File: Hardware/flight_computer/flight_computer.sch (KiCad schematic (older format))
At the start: 38 parts, among them J1 Micro_USB, J2 MicroSD_molex, J3 rpi_zero_w, Q1 PMOS_20V_.76A, Q2 PMOS_20V_.76A, U1 FRAM_128K, U2 STM32F427VITx, U3 MCP131T-300E_TT, Y1 Crystal_24MHZ

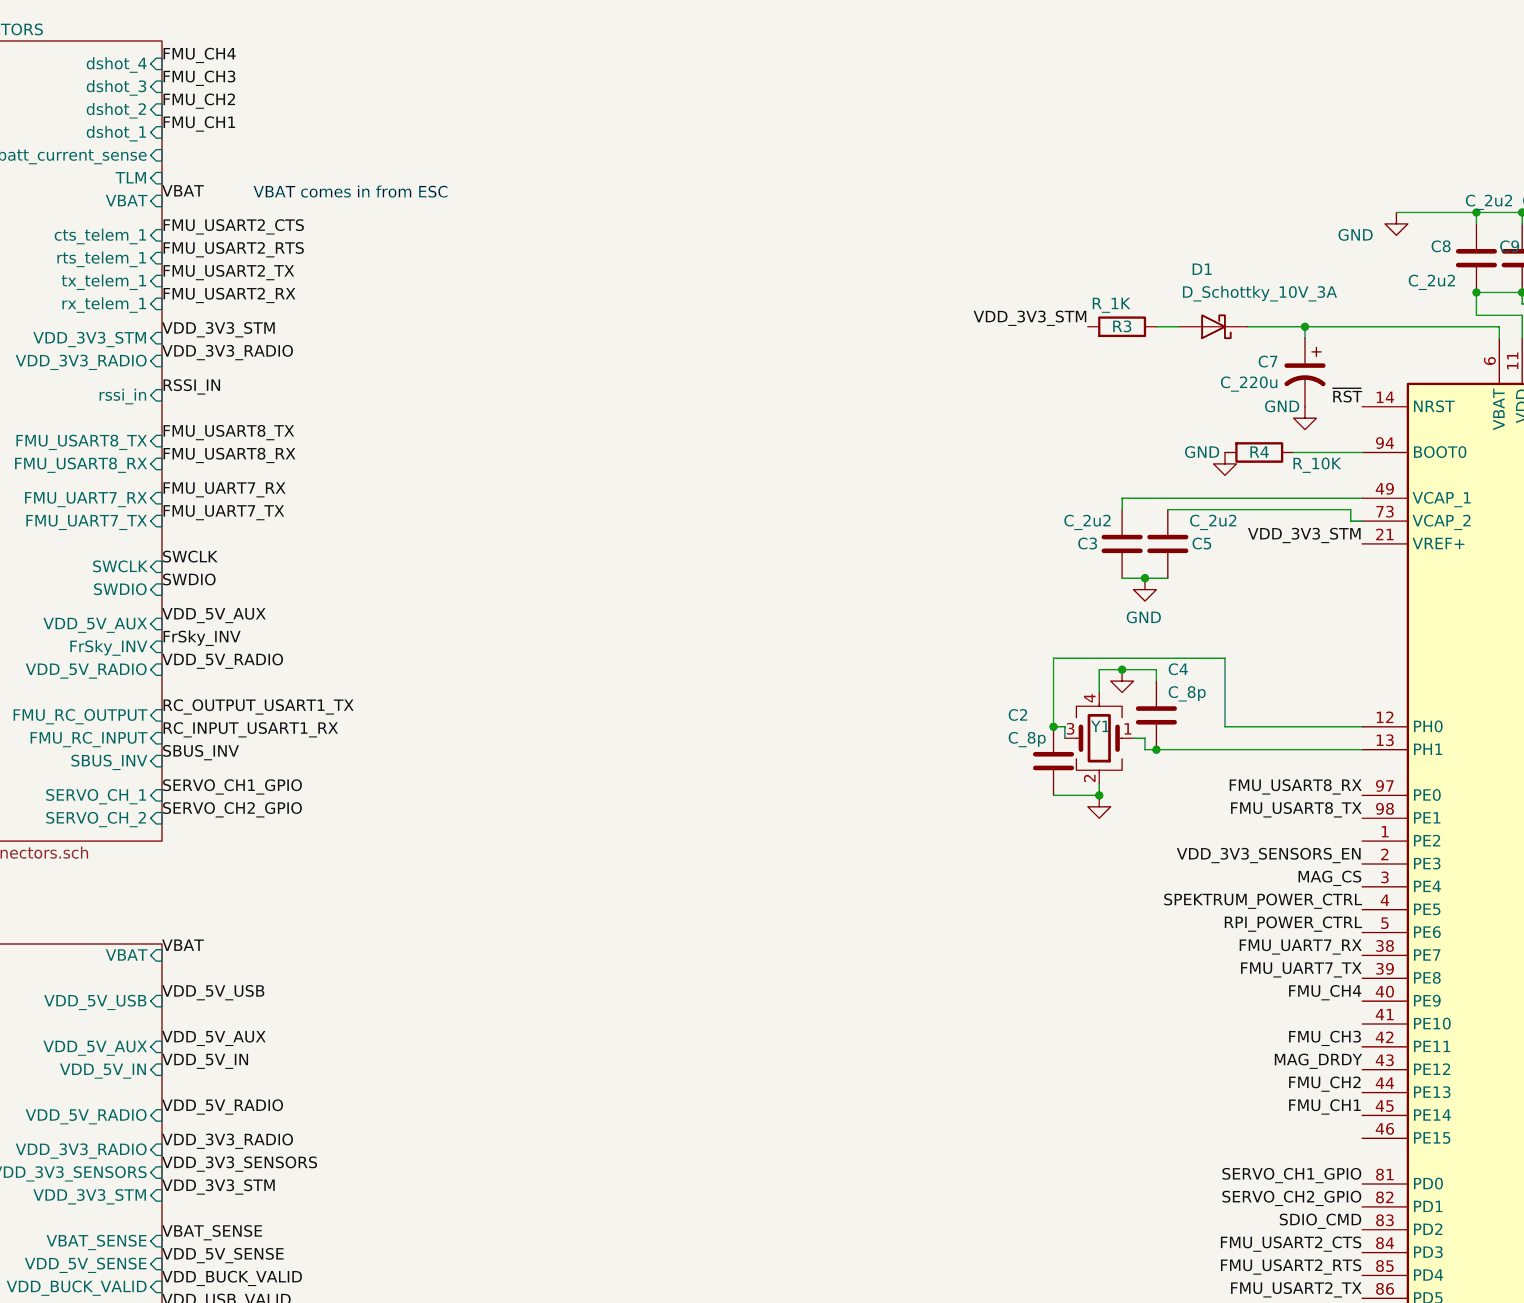
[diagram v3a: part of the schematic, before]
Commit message: Adds remainder esc gpio connections
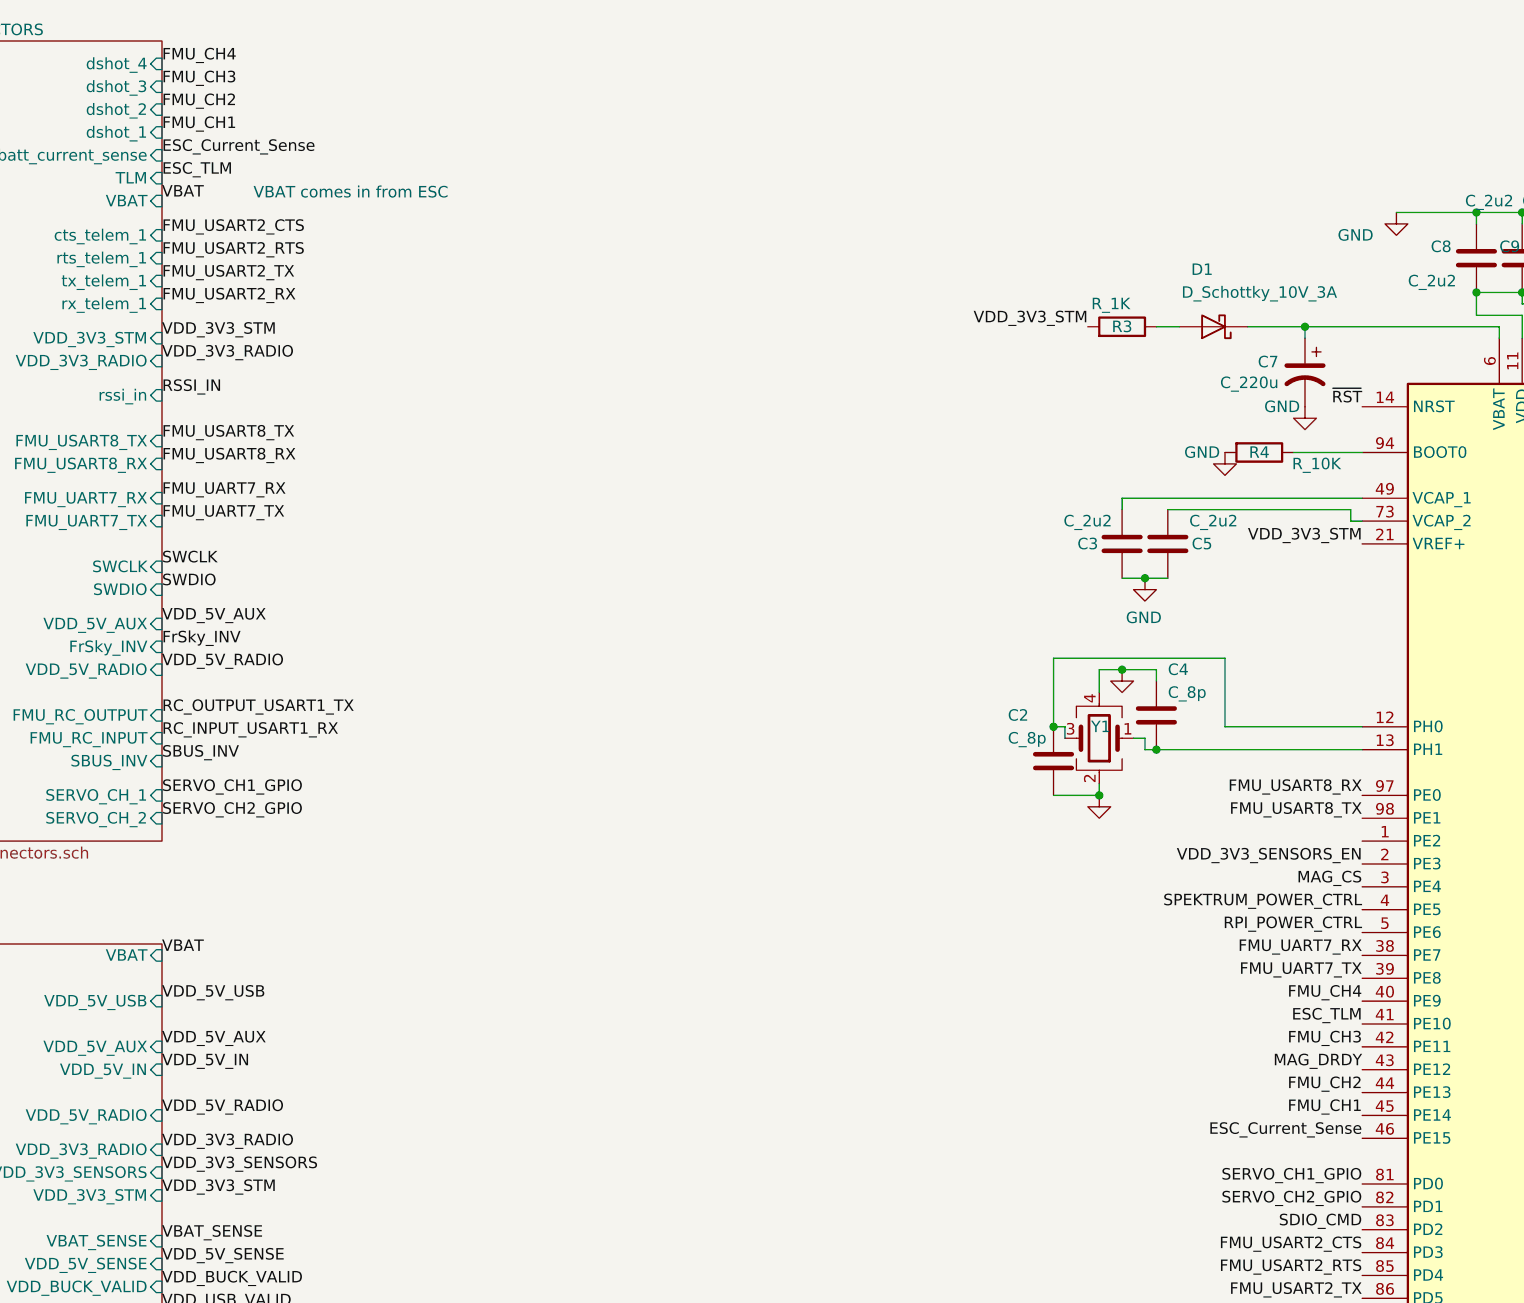
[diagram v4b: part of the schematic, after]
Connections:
- net ESC_TLM: now reaches U2.41 (PE10)
- net ESC_Current_Sense: now reaches U2.46 (PE15)
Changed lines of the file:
@@
 F16 "SWCLK" I R 1700 3000 50
 F17 "SWDIO" I R 1700 3100 50
-F19 "FMU_USART8_TX" I R 1700 2450 50
-F20 "FMU_USART8_RX" I R 1700 2550 50
-F21 "FrSky_INV" I R 1700 3350 50
-F22 "FMU_RC_OUTPUT" I R 1700 3650 50
-F23 "FMU_RC_INPUT" I R 1700 3750 50
-F24 "SBUS_INV" I R 1700 3850 50
-F25 "VDD_5V_RADIO" I R 1700 3450 50
-F26 "VDD_5V_AUX" I R 1700 3250 50
-F27 "SERVO_CH_1" I R 1700 4000 50
-F28 "SERVO_CH_2" I R 1700 4100 50
-F29 "VDD_3V3_RADIO" I R 1700 2100 50
-F30 "VDD_3V3_STM" I R 1700 2000 50
+F18 "FMU_USART8_TX" I R 1700 2450 50
+F19 "FMU_USART8_RX" I R 1700 2550 50
+F20 "FrSky_INV" I R 1700 3350 50
+F21 "FMU_RC_OUTPUT" I R 1700 3650 50
+F22 "FMU_RC_INPUT" I R 1700 3750 50
+F23 "SBUS_INV" I R 1700 3850 50
+F24 "VDD_5V_RADIO" I R 1700 3450 50
+F25 "VDD_5V_AUX" I R 1700 3250 50
+F26 "SERVO_CH_1" I R 1700 4000 50
+F27 "SERVO_CH_2" I R 1700 4100 50
+F28 "VDD_3V3_RADIO" I R 1700 2100 50
+F29 "VDD_3V3_STM" I R 1700 2000 50
 $EndSheet
 Text Label 8750 2600 0    50   ~ 0
@@
 F7 "IMU_INT1_ACCEL" I L 14150 1550 50
 F8 "INT3_GYRO" I L 14150 1650 50
-F10 "MAG_SDO_SA1" I L 14150 2050 50
-F11 "MAG_DRDY" I L 14150 2150 50
-F12 "MAG_CS" I L 14150 2350 50
-F13 "MAG_SDA_SDI_SDO" I L 14150 2450 50
-F14 "MAG_SCL" I L 14150 2550 50
-F15 "BARO_CS" I L 14150 2650 50
-F16 "BARO_MISO" I L 14150 2750 50
-F17 "BARO_MOSI" I L 14150 2850 50
-F18 "BARO_SCK" I L 14150 2950 50
-F19 "GPS_UART_TX" I L 14150 3250 50
-F20 "GPS_UART_RX" I L 14150 3350 50
-F21 "VDD_3V3_SENSORS" I L 14150 3100 50
+F9 "MAG_SDO_SA1" I L 14150 2050 50
+F10 "MAG_DRDY" I L 14150 2150 50
+F11 "MAG_CS" I L 14150 2350 50
+F12 "MAG_SDA_SDI_SDO" I L 14150 2450 50
+F13 "MAG_SCL" I L 14150 2550 50
+F14 "BARO_CS" I L 14150 2650 50
+F15 "BARO_MISO" I L 14150 2750 50
+F16 "BARO_MOSI" I L 14150 2850 50
+F17 "BARO_SCK" I L 14150 2950 50
+F18 "GPS_UART_TX" I L 14150 3250 50
+F19 "GPS_UART_RX" I L 14150 3350 50
+F20 "VDD_3V3_SENSORS" I L 14150 3100 50
 $EndSheet
 Entry Wire Line
@@
 Text Label 6950 5800 2    50   ~ 0
 SERVO_CH2_GPIO
+Text Label 6950 5000 2    50   ~ 0
+ESC_TLM
+Text Label 6950 5500 2    50   ~ 0
+ESC_Current_Sense
+Text Label 1700 1200 0    50   ~ 0
+ESC_Current_Sense
+Text Label 1700 1300 0    50   ~ 0
+ESC_TLM
 $EndSCHEMATC

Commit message: added drone parts
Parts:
- U2: footprint Package_QFP:LQFP-100_14x14mm_P0.5mm -> drone_footprints:QFP50P1600X1600X160-100N
- U3: footprint Package_TO_SOT_SMD:SOT-23 -> TO_SOT_Packages_SMD:SOT-23
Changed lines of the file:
@@
 F 0 "U2" H 7250 1950 50  0000 C CNN
 F 1 "STM32F427VITx" H 7250 2050 50  0000 C CNN
-F 2 "Package_QFP:LQFP-100_14x14mm_P0.5mm" H 7150 2100 50  0001 R CNN
+F 2 "drone_footprints:QFP50P1600X1600X160-100N" H 7150 2100 50  0001 R CNN
 F 3 "http://www.st.com/st-web-ui/static/active/en/resource/technical/document/datasheet/DM00071990.pdf" H 7850 4700 50  0001 C CNN
 	1    7850 4700
@@
 F 0 "U3" V 8700 10650 50  0000 C CNN
 F 1 "MCP131T-300E_TT" V 8600 10650 50  0000 C CNN
-F 2 "Package_TO_SOT_SMD:SOT-23" H 9500 11250 50  0001 C CNN
+F 2 "TO_SOT_Packages_SMD:SOT-23" H 9500 11250 50  0001 C CNN
 F 3 "http://ww1.microchip.com/downloads/en/DeviceDoc/11184d.pdf" H 8850 10650 50  0001 C CNN
 F 4 "MCP131T-300E/TTCT-ND" H 9450 11150 50  0001 C CNN "DPN"

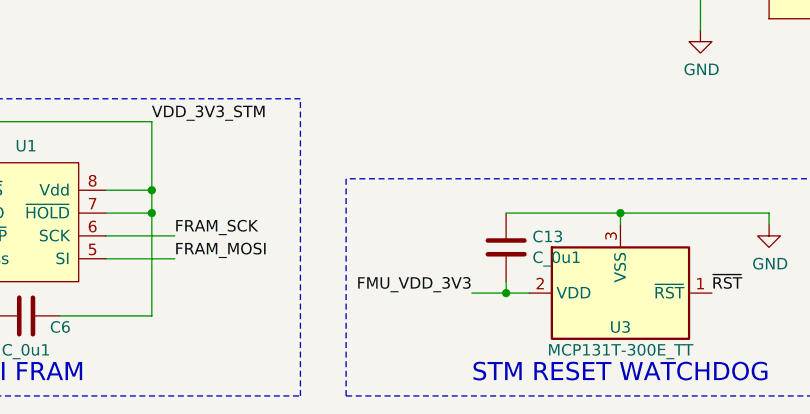
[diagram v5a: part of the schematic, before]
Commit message: Organizes components for layout
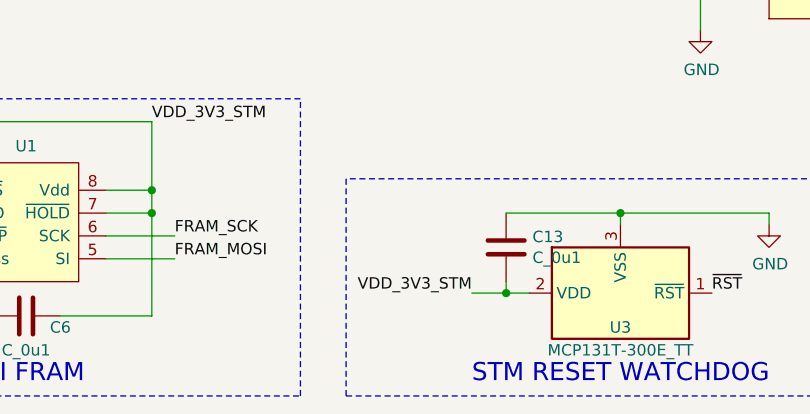
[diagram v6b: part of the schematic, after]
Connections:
- net FMU_VDD_3V3 is gone; now on net VDD_3V3_STM: C13.2, U3.2 (VDD)
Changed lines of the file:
@@
 	8350 10650 8350 10600
 Text Label 8200 10650 2    50   ~ 0
-FMU_VDD_3V3
+VDD_3V3_STM
 Wire Wire Line
 	8350 10650 8200 10650
